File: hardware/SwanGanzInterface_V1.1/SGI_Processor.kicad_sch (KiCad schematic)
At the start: 34 parts, among them J14 Conn_01x03_Pin, J2 Conn_01x09_Pin, SW2 NRST, SW3 UP, SW4 ENTER, SW5 DOWN, SW6 LEFT, SW7 RIGHT, U4 XM0G3507QPMRQ1, Y1 ABM8AIG-40.000MHZ-12-2Z-T3

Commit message: SGI v2 Layout Complete
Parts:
- renumbered C9 to C10, C39 to C11, C10 to C12, C11 to C13, C12 to C14, C13 to C15, C14 to C16, C38 to C9, J14 to J3, R52 to R10, R7 to R11, R8 to R12, R9 to R13, R10 to R14, R11 to R15, R49 to R5, R5 to R6, R50 to R7, R51 to R8, R6 to R9, SW6 to SW2, SW2 to SW3, SW7 to SW4, SW3 to SW5, SW4 to SW6, SW5 to SW7, U4 to U5
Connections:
- no-connect marks 9 -> 10

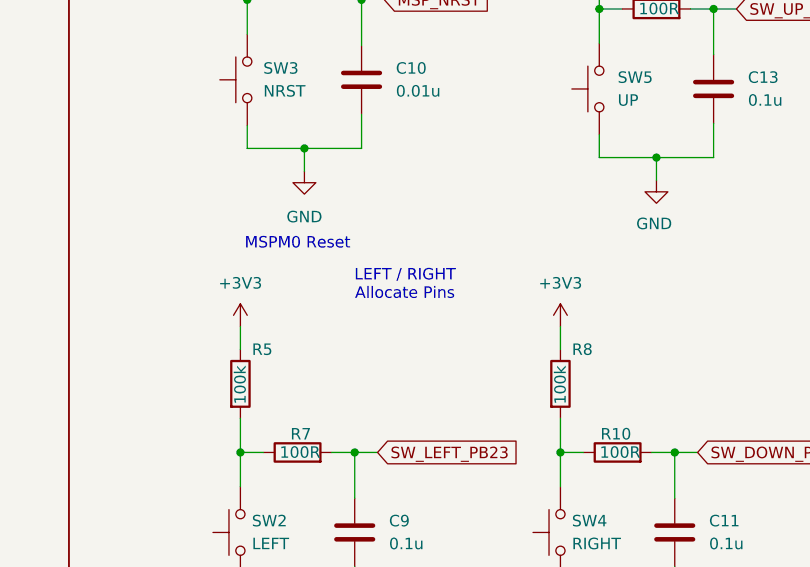
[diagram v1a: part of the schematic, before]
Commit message: Bom changes - purchase request sent
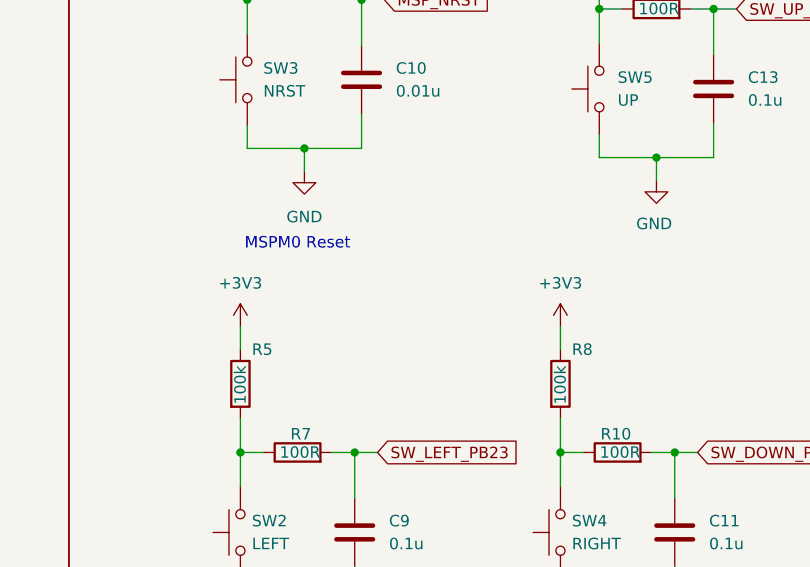
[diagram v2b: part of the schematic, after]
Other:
- note removed: "LEFT / RIGHT Allocate Pins"
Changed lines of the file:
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@@
-		)
-	)
-	(text "LEFT / RIGHT\nAllocate Pins"
-		(exclude_from_sim no)
-		(at 193.548 75.184 0)
-		(effects
-			(font
-				(size 1.27 1.27)
-			)
 		)
 	)
